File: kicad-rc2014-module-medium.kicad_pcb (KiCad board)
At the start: 2 copper layers, 99.1 x 49.9 mm, 2 parts, among them J1 RC2014_Bus

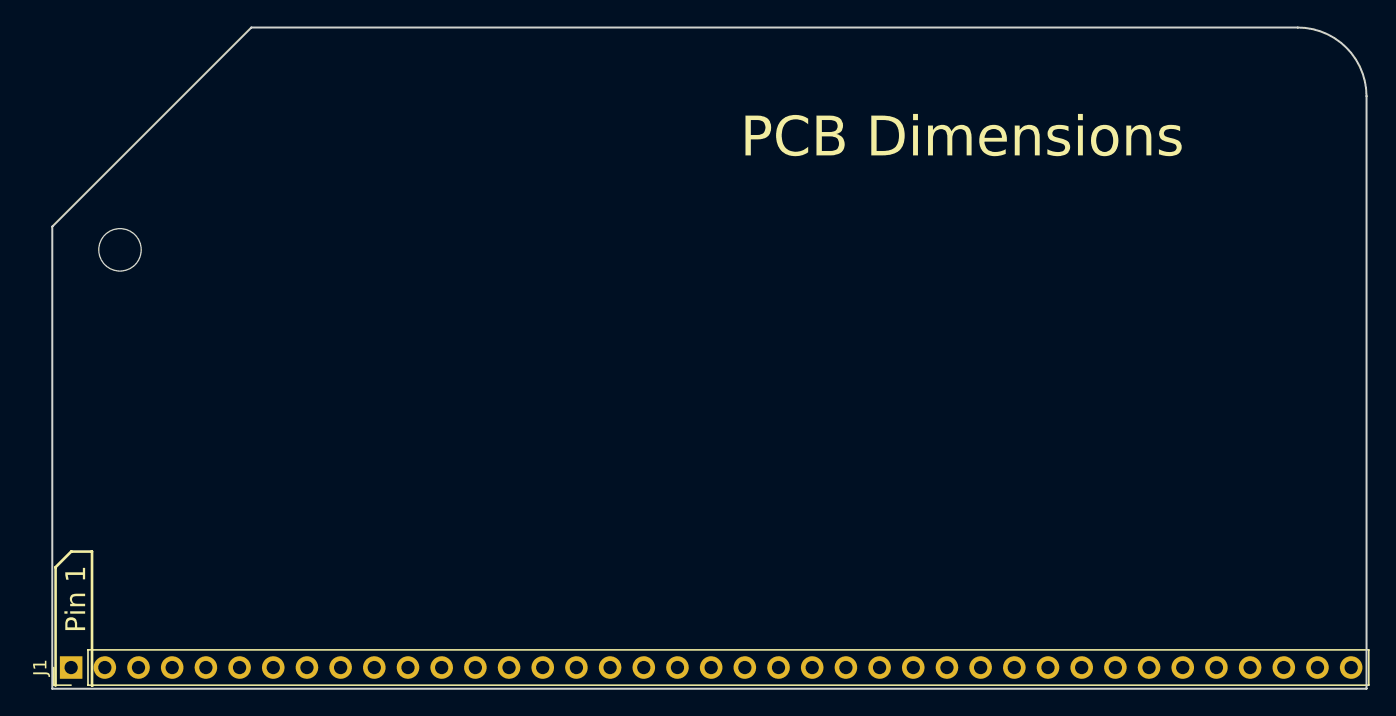
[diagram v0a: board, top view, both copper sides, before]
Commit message: Cleaned up dimensions and moved to correct layers.
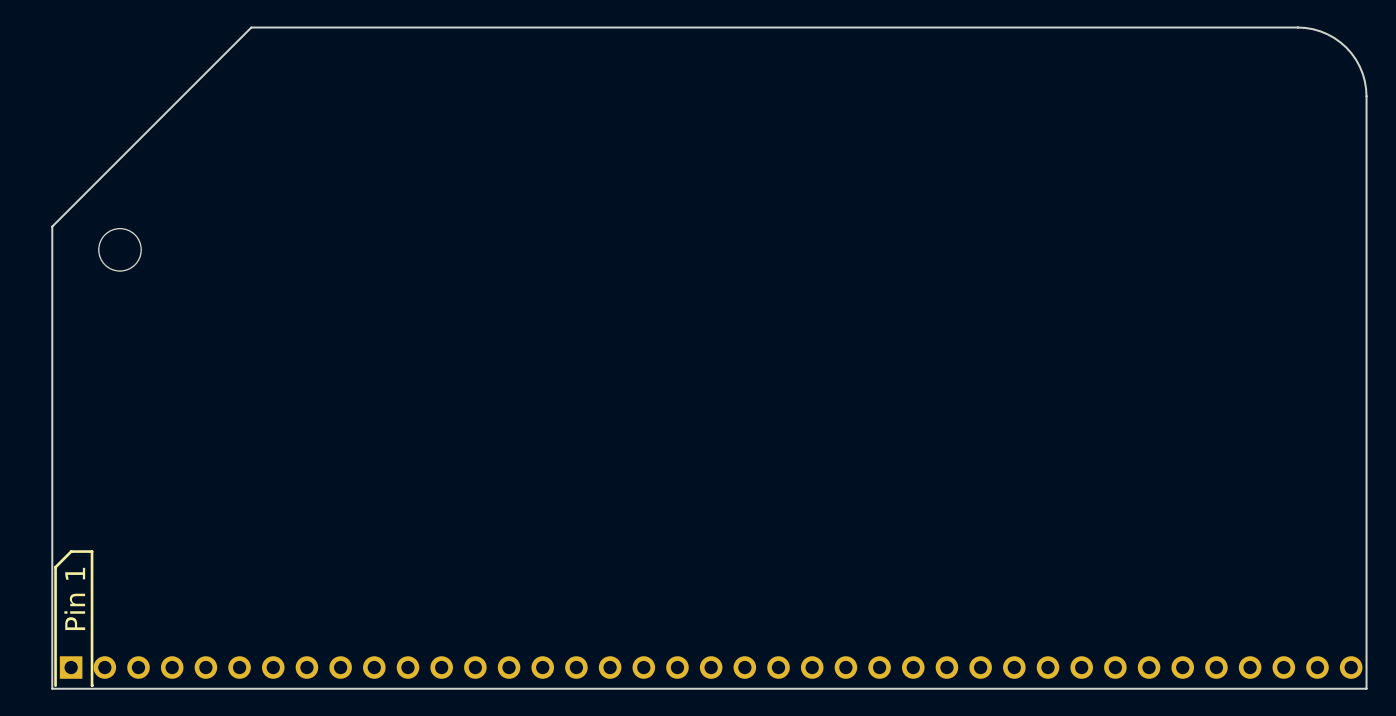
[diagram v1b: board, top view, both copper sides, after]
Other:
- board text added: "135°"
- board text added: "M3 Hole"
- board text added: "PCB Dimensions - RC2014 Medium Module"
- board text removed: "135 deg"
- board text removed: "5.1mm radius"
- board text removed: "M3 Mounting Hole"
- board text removed: "PCB Dimensions"
